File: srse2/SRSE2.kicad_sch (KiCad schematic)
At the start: 87 parts, among them J1 s88-N, J2 CAN, J3 Hanrun HR911105A, P1 I2S, P10 PIC_SPARE, P11 RS485 TERM, P12 RS485, P13 CONN_01X03, P15 RA5, P17 RA5, P18 CONN_01X03, P19 CONN_01X02, P2 CONN_01X09, P20 O2P-Rst, P3 CONN_01X02, P4 CONN_01X04, P5 CONN_01X04, P6 ISO_I2C, P7 CAN_TERM, P8 CAN, P9 PIC_I2C, U1 Omega2, U2 ADuM1250, U3 SN65HVD230, U4 PIC18F25K80, U6 MAX485, U7 TPS5430DDA, U8 CD4504, U9 LM317, Y1 16MHz

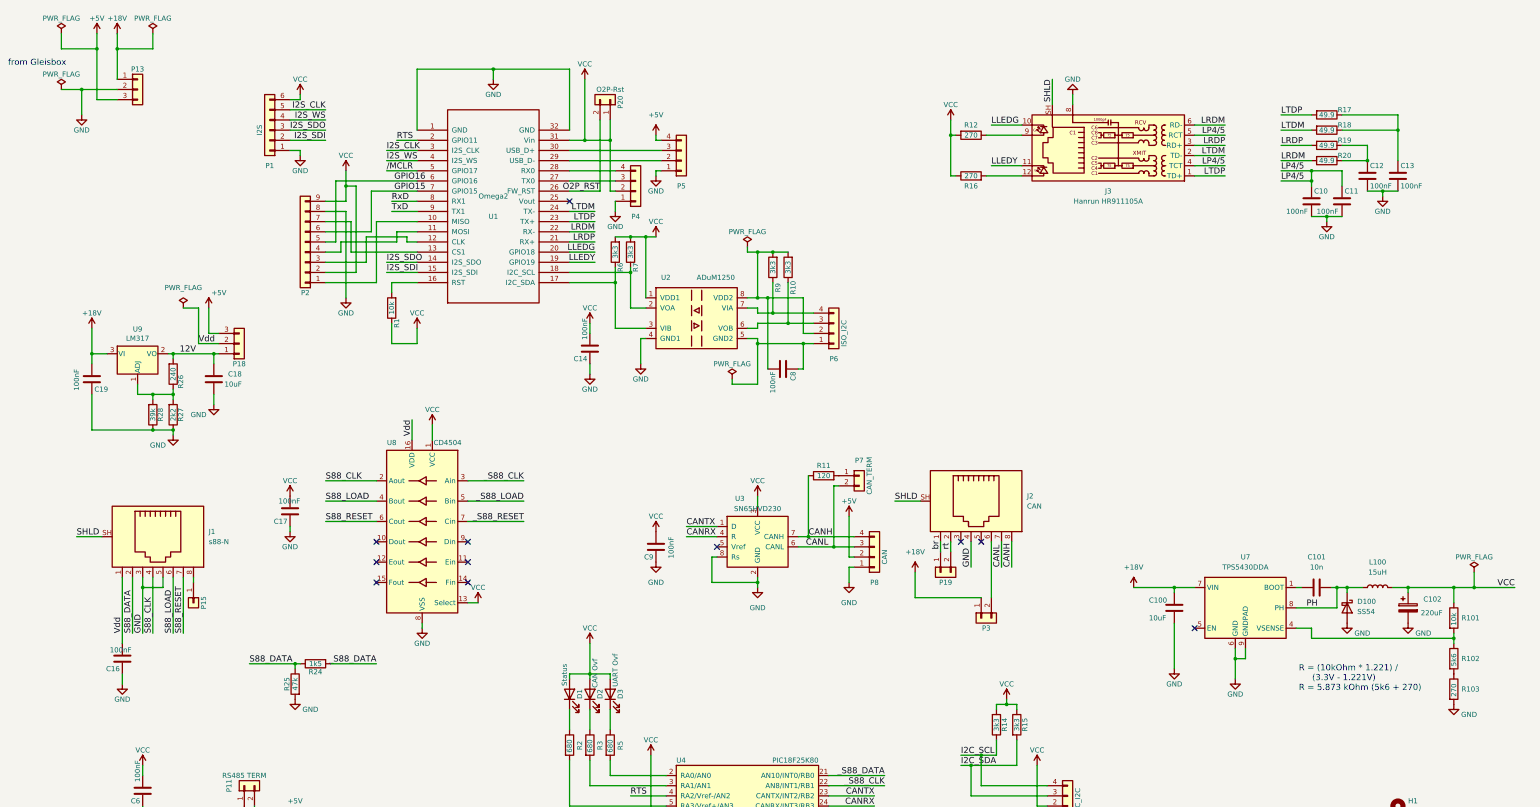
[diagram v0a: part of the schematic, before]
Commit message: reorganize schematic
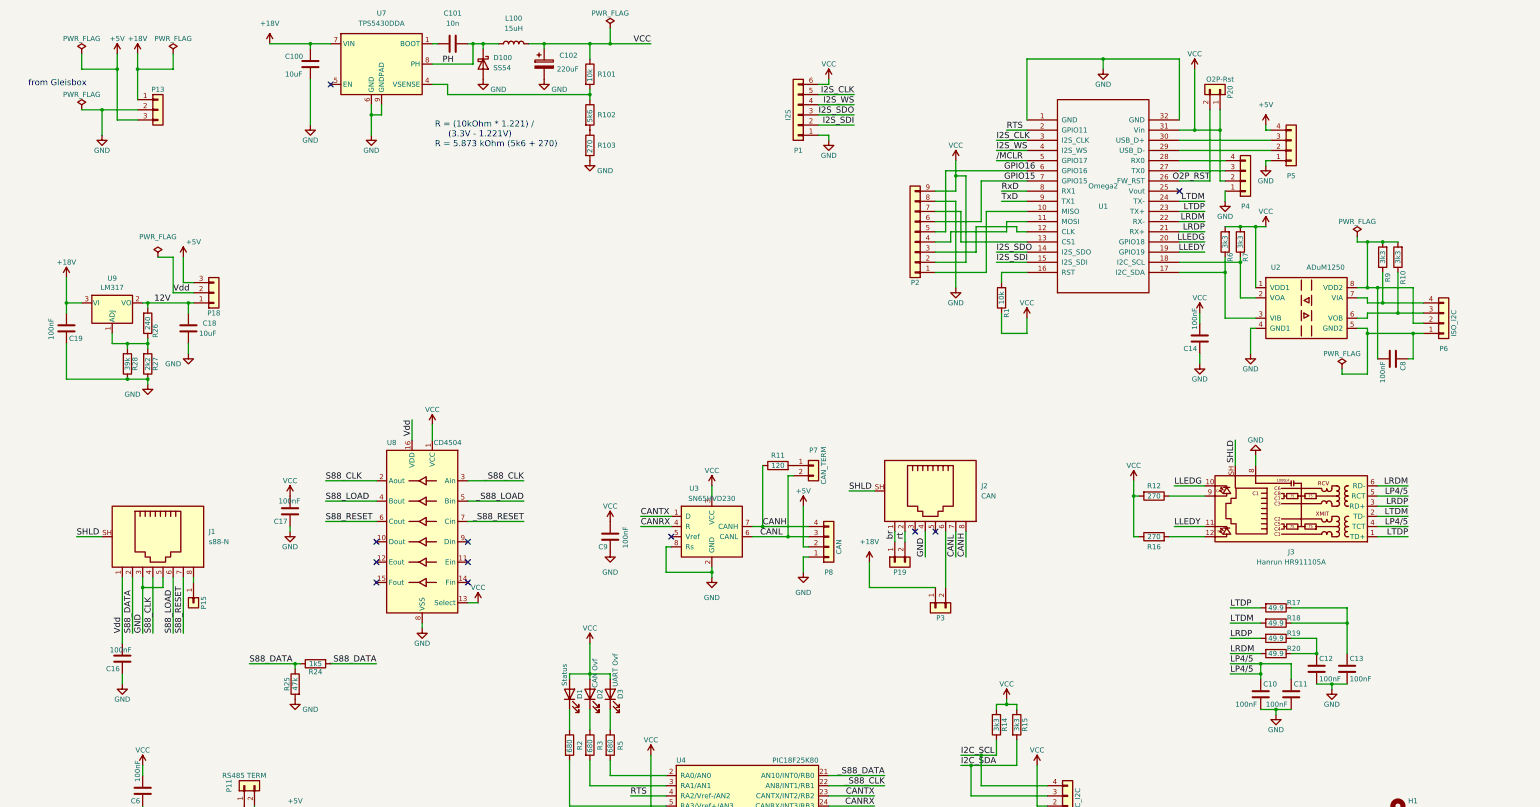
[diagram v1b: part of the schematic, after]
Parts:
- U1: now left out of the parts list
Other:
- moved on the sheet: C10, C100, C101, C102, C11, C12, C13, C14, C18, C19, C8, C9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

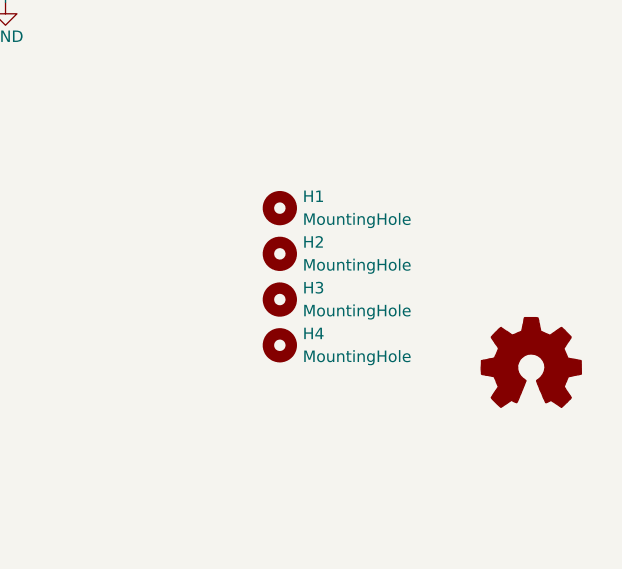
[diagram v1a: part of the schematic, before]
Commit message: git rid off warning
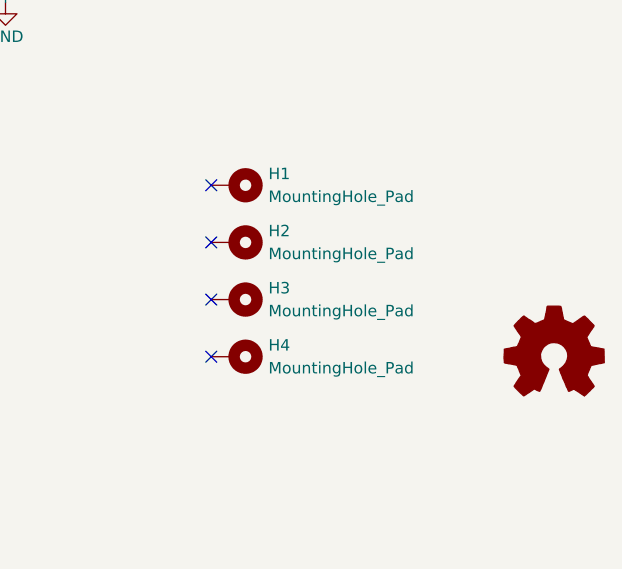
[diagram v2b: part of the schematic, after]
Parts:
- removed H1, H2, H3, H4: MountingHole, srse2:MountingHole_3mm, symbol Mechanical:MountingHole
- added H1, H2, H3, H4: MountingHole_Pad, srse2:MountingHole_3mm, symbol Mechanical:MountingHole_Pad
- added SYM1: Logo_Open_Hardware_Small, srse2:CC_Logo, symbol Graphic:Logo_Open_Hardware_Small
- J2: footprint srse2:MEBP_8-8G -> srse2:MEBP_8-8G_1
- U8: footprint Package_SO:SO-16_3.9x9.9mm_P1.27mm -> Package_SO:SOIC-16_3.9x9.9mm_P1.27mm
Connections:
- no-connect marks 11 -> 15

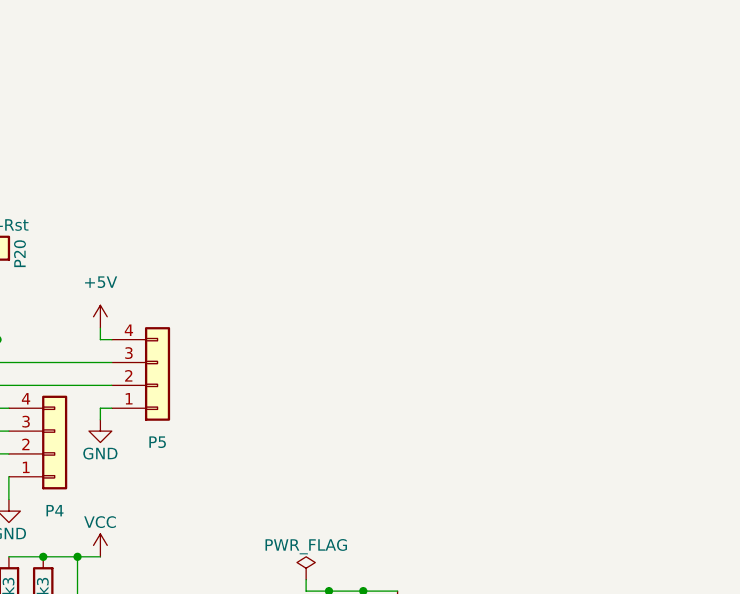
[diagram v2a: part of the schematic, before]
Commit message: add Omega2 sockets
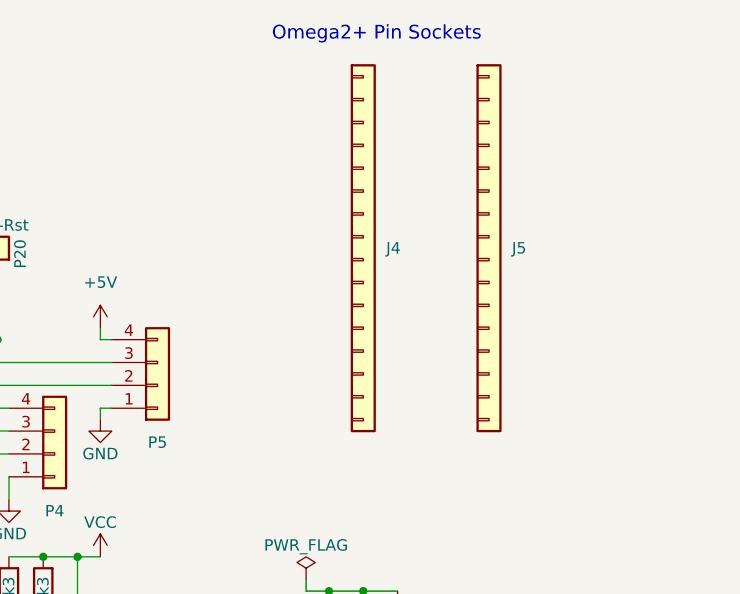
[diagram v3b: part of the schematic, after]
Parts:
- added J4, J5: ~, srse2:Conn16, symbol srse2:Conn16
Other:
- note added: "Omega2+ Pin Sockets"
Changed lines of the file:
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@@
   (title_block
     (title "Smallest Rocrail Server Ever II")
-    (date "2024-04-11")
+    (date "2024-04-13")
     (rev "1.82")
     (company "Gerhard Bertelsmann")
@@
     (effects (font (size 1.524 1.524)) (justify left bottom))
   )
+  (text "Omega2+ Pin Sockets" (at 353.06 26.67 0)
+    (effects (font (size 1.524 1.524)) (justify left bottom))
+  )
   (label "TxD" (at 232.41 238.76 180) (fields_autoplaced)
     (effects (font (size 1.524 1.524)) (justify right bottom))
@@
     )
   )
+  (symbol (lib_id "srse2:Conn16") (at 363.22 49.53 0) (unit 1)
+    (in_bom yes) (on_board yes) (dnp no) (fields_autoplaced)
+    (property "Reference" "J4" (at 365.76 49.53 0)
+      (effects (font (size 1.27 1.27)) (justify left))
+    )
+    (property "Value" "~" (at 363.22 49.53 0)
+      (effects (font (size 1.27 1.27)))
+    )
+    (property "Footprint" "srse2:Conn16" (at 363.22 49.53 0)
+      (effects (font (size 1.27 1.27)) hide)
+    )
+    (property "Datasheet" "" (at 363.22 49.53 0)
+      (effects (font (size 1.27 1.27)) hide)
+    )
+    (property "LCSC" "C2938437" (at 363.22 49.53 0)
+      (effects (font (size 1.524 1.524)) hide)
+    )
+    (instances
+      (project "SRSE2"
+        (path "/2fb9dd88-7f2e-4e94-830f-18cb5a9434c7"
+          (reference "J4") (unit 1)
+        )
+      )
+    )
+  )
   (symbol (lib_name "VCC_1") (lib_id "power:VCC") (at 170.18 157.48 0) (unit 1)
     (in_bom yes) (on_board yes) (dnp no)
@@
         )
       )
+    )
+  )
+  (symbol (lib_id "srse2:Conn16") (at 377.19 49.53 0) (unit 1)
+    (in_bom yes) (on_board yes) (dnp no) (fields_autoplaced)
+    (property "Reference" "J5" (at 379.73 49.53 0)
+      (effects (font (size 1.27 1.27)) (justify left))
+    )
+    (property "Value" "~" (at 377.19 49.53 0)
+      (effects (font (size 1.27 1.27)))
+    )
+    (property "Footprint" "srse2:Conn16" (at 377.19 49.53 0)
+      (effects (font (size 1.27 1.27)) hide)
+    )
+    (property "Datasheet" "" (at 377.19 49.53 0)
+      (effects (font (size 1.27 1.27)) hide)
+    )
+    (property "LCSC" "C2938437" (at 377.19 49.53 0)
+      (effects (font (size 1.524 1.524)) hide)
+    )
+    (instances
+      (project "SRSE2"
+        (path "/2fb9dd88-7f2e-4e94-830f-18cb5a9434c7"
+          (reference "J5") (unit 1)
+        )
+      )

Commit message: fix ERC/DRC errors and warnings / fix bom and placements
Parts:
- H1, H2, H3, H4, J3, P19, P3: now left out of the parts list
- J4, J5: JLCRotOffset (none) -> 90
- U7: footprint Package_SO:TI_SO-PowerPAD-8_ThermalVias -> srse2:TI_SO-PowerPAD-8_ThermalVias
- U9: JLCPCB Position Offset (none) -> -1.8,0.0
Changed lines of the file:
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@@
   )
   (symbol (lib_id "Connector_Generic:Conn_01x02") (at 241.3 167.64 90) (mirror x) (unit 1)
-    (in_bom yes) (on_board yes) (dnp no)
+    (in_bom no) (on_board yes) (dnp no)
     (property "Reference" "P19" (at 242.57 170.18 90)
       (effects (font (size 1.27 1.27)))
@@
   )
   (symbol (lib_id "Connector_Generic:Conn_01x02") (at 251.46 179.07 90) (mirror x) (unit 1)
-    (in_bom yes) (on_board yes) (dnp no)
+    (in_bom no) (on_board yes) (dnp no)
     (property "Reference" "P3" (at 252.73 181.61 90)
       (effects (font (size 1.27 1.27)))
@@
       (effects (font (size 1.27 1.27)) hide)
     )
+    (property "JLCPCB Position Offset" "-1.8,0.0" (at 45.72 102.87 0)
+      (effects (font (size 1.524 1.524)) hide)
+    )
     (pin "1")
     (pin "2")
@@
   )
   (symbol (lib_id "Connector:RJ45_Hanrun_HR911105A_Horizontal") (at 341.63 153.67 180) (unit 1)
-    (in_bom yes) (on_board yes) (dnp no) (fields_autoplaced)
+    (in_bom no) (on_board yes) (dnp no) (fields_autoplaced)
     (property "Reference" "J3" (at 340.36 165.1 0)
       (effects (font (size 1.27 1.27)))
@@
       (effects (font (size 1.27 1.27)))
     )
-    (property "Footprint" "Package_SO:TI_SO-PowerPAD-8_ThermalVias" (at 114.3 52.07 0)
+    (property "Footprint" "srse2:TI_SO-PowerPAD-8_ThermalVias" (at 114.3 52.07 0)
       (effects (font (size 1.27 1.27) italic) (justify left) hide)
     )
@@
       (effects (font (size 1.524 1.524)) hide)
     )
+    (property "JLCRotOffset" "90" (at 363.22 49.53 0)
+      (effects (font (size 1.524 1.524)) hide)
+    )
     (instances
       (project "SRSE2"
@@
     )
     (property "LCSC" "C2938437" (at 377.19 49.53 0)
+      (effects (font (size 1.524 1.524)) hide)
+    )
+    (property "JLCRotOffset" "90" (at 377.19 49.53 0)
       (effects (font (size 1.524 1.524)) hide)
     )
@@
   )
   (symbol (lib_id "Mechanical:MountingHole_Pad") (at 361.95 232.41 270) (unit 1)
-    (in_bom yes) (on_board yes) (dnp no) (fields_autoplaced)
+    (in_bom no) (on_board yes) (dnp no) (fields_autoplaced)
     (property "Reference" "H2" (at 365.76 231.14 90)
       (effects (font (size 1.27 1.27)) (justify left))
@@
   )
   (symbol (lib_id "Mechanical:MountingHole_Pad") (at 361.95 238.76 270) (unit 1)
-    (in_bom yes) (on_board yes) (dnp no) (fields_autoplaced)
+    (in_bom no) (on_board yes) (dnp no) (fields_autoplaced)
     (property "Reference" "H3" (at 365.76 237.49 90)
       (effects (font (size 1.27 1.27)) (justify left))
@@
   )
   (symbol (lib_id "Mechanical:MountingHole_Pad") (at 361.95 245.11 270) (unit 1)
-    (in_bom yes) (on_board yes) (dnp no) (fields_autoplaced)
+    (in_bom no) (on_board yes) (dnp no) (fields_autoplaced)
     (property "Reference" "H4" (at 365.76 243.84 90)
       (effects (font (size 1.27 1.27)) (justify left))
@@
   )
   (symbol (lib_id "Mechanical:MountingHole_Pad") (at 361.95 226.06 270) (unit 1)
-    (in_bom yes) (on_board yes) (dnp no) (fields_autoplaced)
+    (in_bom no) (on_board yes) (dnp no) (fields_autoplaced)
     (property "Reference" "H1" (at 365.76 224.79 90)
       (effects (font (size 1.27 1.27)) (justify left))

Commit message: fix local library issue
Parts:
- P11, P19, P7: footprint Connector_PinSocket_2.54mm:PinSocket_1x02_P2.54mm_Vertical -> Connector_PinHeader_2.54mm:PinHeader_1x02_P2.54mm_Vertical
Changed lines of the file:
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@@
       (effects (font (size 1.27 1.27)))
     )
-    (property "Footprint" "Connector_PinSocket_2.54mm:PinSocket_1x02_P2.54mm_Vertical" (at 78.74 223.52 0)
+    (property "Footprint" "Connector_PinHeader_2.54mm:PinHeader_1x02_P2.54mm_Vertical" (at 78.74 223.52 0)
       (effects (font (size 1.27 1.27)) hide)
     )
@@
       (effects (font (size 1.27 1.27)))
     )
-    (property "Footprint" "Connector_PinSocket_2.54mm:PinSocket_1x02_P2.54mm_Vertical" (at 220.98 143.51 0)
+    (property "Footprint" "Connector_PinHeader_2.54mm:PinHeader_1x02_P2.54mm_Vertical" (at 220.98 143.51 0)
       (effects (font (size 1.27 1.27)) hide)
     )
@@
       (effects (font (size 1.27 1.27)) hide)
     )
-    (property "Footprint" "Connector_PinSocket_2.54mm:PinSocket_1x02_P2.54mm_Vertical" (at 241.3 167.64 0)
-      (effects (font (size 1.27 1.27)) hide)
-    )
+    (property "Footprint" "Connector_PinHeader_2.54mm:PinHeader_1x02_P2.54mm_Vertical" (at 241.3 167.64 0)
+      (effects (font (size 1.27 1.27)) hide)
+    )

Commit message: switch 18pF caps from 0805 to 0603 for JLCPCB basic parts
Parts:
- C3, C4: footprint Capacitor_SMD:C_0805_2012Metric -> Capacitor_SMD:C_0603_1608Metric; LCSC C1797 -> C1647
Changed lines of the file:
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@@
       (effects (font (size 1.27 1.27)) (justify left))
     )
-    (property "Footprint" "Capacitor_SMD:C_0805_2012Metric" (at 153.3652 259.08 0)
+    (property "Footprint" "Capacitor_SMD:C_0603_1608Metric" (at 153.3652 259.08 0)
       (effects (font (size 1.27 1.27)) hide)
     )
@@
       (effects (font (size 1.27 1.27)))
     )
-    (property "LCSC" "C1797" (at 152.4 255.27 0)
+    (property "LCSC" "C1647" (at 152.4 255.27 0)
       (effects (font (size 1.27 1.27)) hide)
     )
@@
       (effects (font (size 1.27 1.27)) (justify left))
     )
-    (property "Footprint" "Capacitor_SMD:C_0805_2012Metric" (at 164.7952 259.08 0)
+    (property "Footprint" "Capacitor_SMD:C_0603_1608Metric" (at 164.7952 259.08 0)
       (effects (font (size 1.27 1.27)) hide)
     )
@@
       (effects (font (size 1.27 1.27)))
     )
-    (property "LCSC" "C1797" (at 163.83 255.27 0)
+    (property "LCSC" "C1647" (at 163.83 255.27 0)
       (effects (font (size 1.27 1.27)) hide)
     )

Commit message: more cutting costs
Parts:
- R12, R16: footprint Resistor_SMD:R_0805_2012Metric_Pad1.20x1.40mm_HandSolder -> Resistor_SMD:R_0603_1608Metric_Pad0.98x0.95mm_HandSolder; LCSC C17590 -> C22966
- R26: footprint Resistor_SMD:R_0805_2012Metric_Pad1.20x1.40mm_HandSolder -> Resistor_SMD:R_0603_1608Metric_Pad0.98x0.95mm_HandSolder; LCSC C17572 -> C23350
- R27: footprint Resistor_SMD:R_0805_2012Metric_Pad1.20x1.40mm_HandSolder -> Resistor_SMD:R_0603_1608Metric_Pad0.98x0.95mm_HandSolder; LCSC C17520 -> C4190
- R28: footprint Resistor_SMD:R_0805_2012Metric_Pad1.20x1.40mm_HandSolder -> Resistor_SMD:R_0603_1608Metric_Pad0.98x0.95mm_HandSolder; LCSC C25826 -> C23153
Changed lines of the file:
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@@
       (effects (font (size 1.27 1.27)))
     )
-    (property "Footprint" "Resistor_SMD:R_0805_2012Metric_Pad1.20x1.40mm_HandSolder" (at 306.07 163.068 0)
+    (property "Footprint" "Resistor_SMD:R_0603_1608Metric_Pad0.98x0.95mm_HandSolder" (at 306.07 163.068 0)
       (effects (font (size 1.27 1.27)) hide)
     )
@@
       (effects (font (size 1.27 1.27)))
     )
-    (property "LCSC" "C17590" (at 306.07 161.29 90)
+    (property "LCSC" "C22966" (at 306.07 161.29 90)
       (effects (font (size 1.27 1.27)) hide)
     )
@@
       (effects (font (size 1.27 1.27)))
     )
-    (property "Footprint" "Resistor_SMD:R_0805_2012Metric_Pad1.20x1.40mm_HandSolder" (at 306.07 149.352 0)
+    (property "Footprint" "Resistor_SMD:R_0603_1608Metric_Pad0.98x0.95mm_HandSolder" (at 306.07 149.352 0)
       (effects (font (size 1.27 1.27)) hide)
     )
@@
       (effects (font (size 1.27 1.27)))
     )
-    (property "LCSC" "C17590" (at 306.07 151.13 90)
+    (property "LCSC" "C22966" (at 306.07 151.13 90)
       (effects (font (size 1.27 1.27)) hide)
     )
@@
       (effects (font (size 1.27 1.27)))
     )
-    (property "Footprint" "Resistor_SMD:R_0805_2012Metric_Pad1.20x1.40mm_HandSolder" (at 52.832 107.95 0)
+    (property "Footprint" "Resistor_SMD:R_0603_1608Metric_Pad0.98x0.95mm_HandSolder" (at 52.832 107.95 0)
       (effects (font (size 1.27 1.27)) hide)
     )
@@
       (effects (font (size 1.27 1.27)))
     )
-    (property "LCSC" "C17572" (at 54.61 107.95 90)
+    (property "LCSC" "C23350" (at 54.61 107.95 90)
       (effects (font (size 1.27 1.27)) hide)
     )
@@
       (effects (font (size 1.27 1.27)))
     )
-    (property "Footprint" "Resistor_SMD:R_0805_2012Metric_Pad1.20x1.40mm_HandSolder" (at 52.832 118.11 0)
+    (property "Footprint" "Resistor_SMD:R_0603_1608Metric_Pad0.98x0.95mm_HandSolder" (at 52.832 118.11 0)
       (effects (font (size 1.27 1.27)) hide)
     )
@@
       (effects (font (size 1.27 1.27)))
     )
-    (property "LCSC" "C17520" (at 54.61 118.11 90)
+    (property "LCSC" "C4190" (at 54.61 118.11 90)
       (effects (font (size 1.27 1.27)) hide)
     )
@@
       (effects (font (size 1.27 1.27)))
     )
-    (property "Footprint" "Resistor_SMD:R_0805_2012Metric_Pad1.20x1.40mm_HandSolder" (at 47.752 118.11 0)
+    (property "Footprint" "Resistor_SMD:R_0603_1608Metric_Pad0.98x0.95mm_HandSolder" (at 47.752 118.11 0)
       (effects (font (size 1.27 1.27)) hide)
     )
@@
       (effects (font (size 1.27 1.27)))
     )
-    (property "LCSC" "C25826" (at 49.53 118.11 90)
-      (effects (font (size 1.27 1.27)) hide)
-    )
+    (property "LCSC" "C23153" (at 49.53 118.11 90)
+      (effects (font (size 1.27 1.27)) hide)
+    )

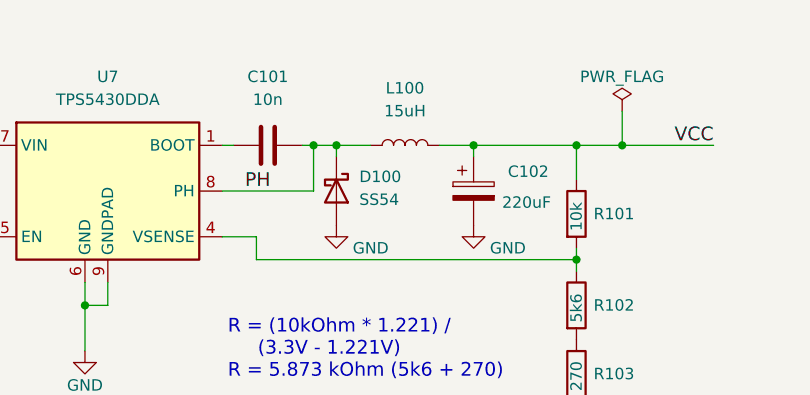
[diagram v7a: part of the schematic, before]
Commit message: 15uH isn't available at JLCPCB - use 18uH instead
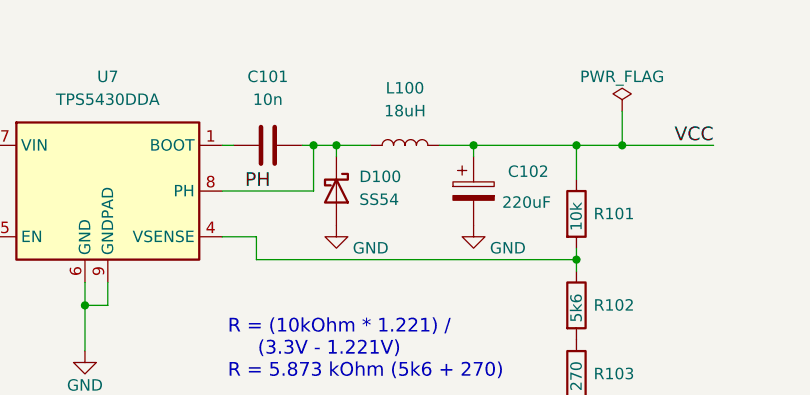
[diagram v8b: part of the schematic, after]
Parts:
- L100: value 15uH -> 18uH; LCSC C225048 -> C225049; LCSC_A (none) -> C225048 15uH C225049 18uH
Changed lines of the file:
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@@
       (effects (font (size 1.27 1.27)))
     )
-    (property "Value" "15uH" (at 146.05 34.29 90)
+    (property "Value" "18uH" (at 146.05 34.29 90)
       (effects (font (size 1.27 1.27)))
     )
@@
       (effects (font (size 1.27 1.27)) hide)
     )
-    (property "LCSC" "C225048" (at 146.05 38.1 90)
+    (property "LCSC" "C225049" (at 146.05 38.1 90)
       (effects (font (size 1.524 1.524)) hide)
     )
+    (property "LCSC_A" "C225048 15uH C225049 18uH " (at 146.05 38.1 90)
+      (effects (font (size 1.524 1.524)) hide)
+    )
